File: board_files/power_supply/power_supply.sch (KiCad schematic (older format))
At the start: 4 parts

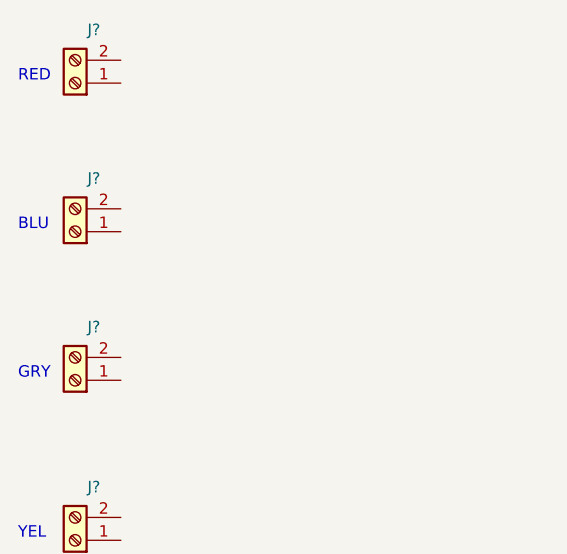
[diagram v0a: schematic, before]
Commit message: Added bridge rectifiers
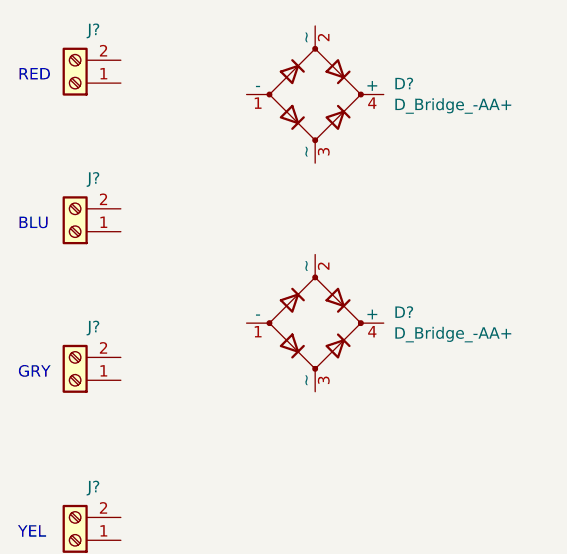
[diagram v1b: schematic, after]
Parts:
- added D? (x2): D_Bridge_-AA+, Diode_THT:Diode_Bridge_32.0x5.6x17.0mm_P10.0mm_P7.5mm, symbol Device:D_Bridge_-AA+
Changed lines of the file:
@@
 EESchema Schematic File Version 4
+LIBS:power_supply-cache
 EELAYER 29 0
 EELAYER END
@@
 Text Notes 3700 4750 0    50   ~ 0
 YEL\n
+$Comp
+L Device:D_Bridge_-AA+ D?
+U 1 1 5EFB3361
+P 5000 2800
+F 0 "D?" H 5344 2846 50  0000 L CNN
+F 1 "D_Bridge_-AA+" H 5344 2755 50  0000 L CNN
+F 2 "Diode_THT:Diode_Bridge_32.0x5.6x17.0mm_P10.0mm_P7.5mm" H 5000 2800 50  0001 C CNN
+F 3 "~" H 5000 2800 50  0001 C CNN
+F 4 "BRIDGE RECT 1PHASE 800V 25A GBJ" H 5000 2800 50  0001 C CNN "Description"
+F 5 "GBJ2508-BP" H 5000 2800 50  0001 C CNN "MPN"
+F 6 "GBJ2508-BPMS-ND" H 5000 2800 50  0001 C CNN "Digikey PN"
+	1    5000 2800
+	1    0    0    -1
+$EndComp
+$Comp
+L Device:D_Bridge_-AA+ D?
+U 1 1 5EFB44A5
+P 5000 3800
+F 0 "D?" H 5344 3846 50  0000 L CNN
+F 1 "D_Bridge_-AA+" H 5344 3755 50  0000 L CNN
+F 2 "Diode_THT:Diode_Bridge_32.0x5.6x17.0mm_P10.0mm_P7.5mm" H 5000 3800 50  0001 C CNN
+F 3 "~" H 5000 3800 50  0001 C CNN
+F 4 "BRIDGE RECT 1PHASE 800V 25A GBJ" H 5000 3800 50  0001 C CNN "Description"
+F 5 "GBJ2508-BP" H 5000 3800 50  0001 C CNN "MPN"
+F 6 "GBJ2508-BPMS-ND" H 5000 3800 50  0001 C CNN "Digikey PN"
+	1    5000 3800
+	1    0    0    -1
+$EndComp
 $EndSCHEMATC

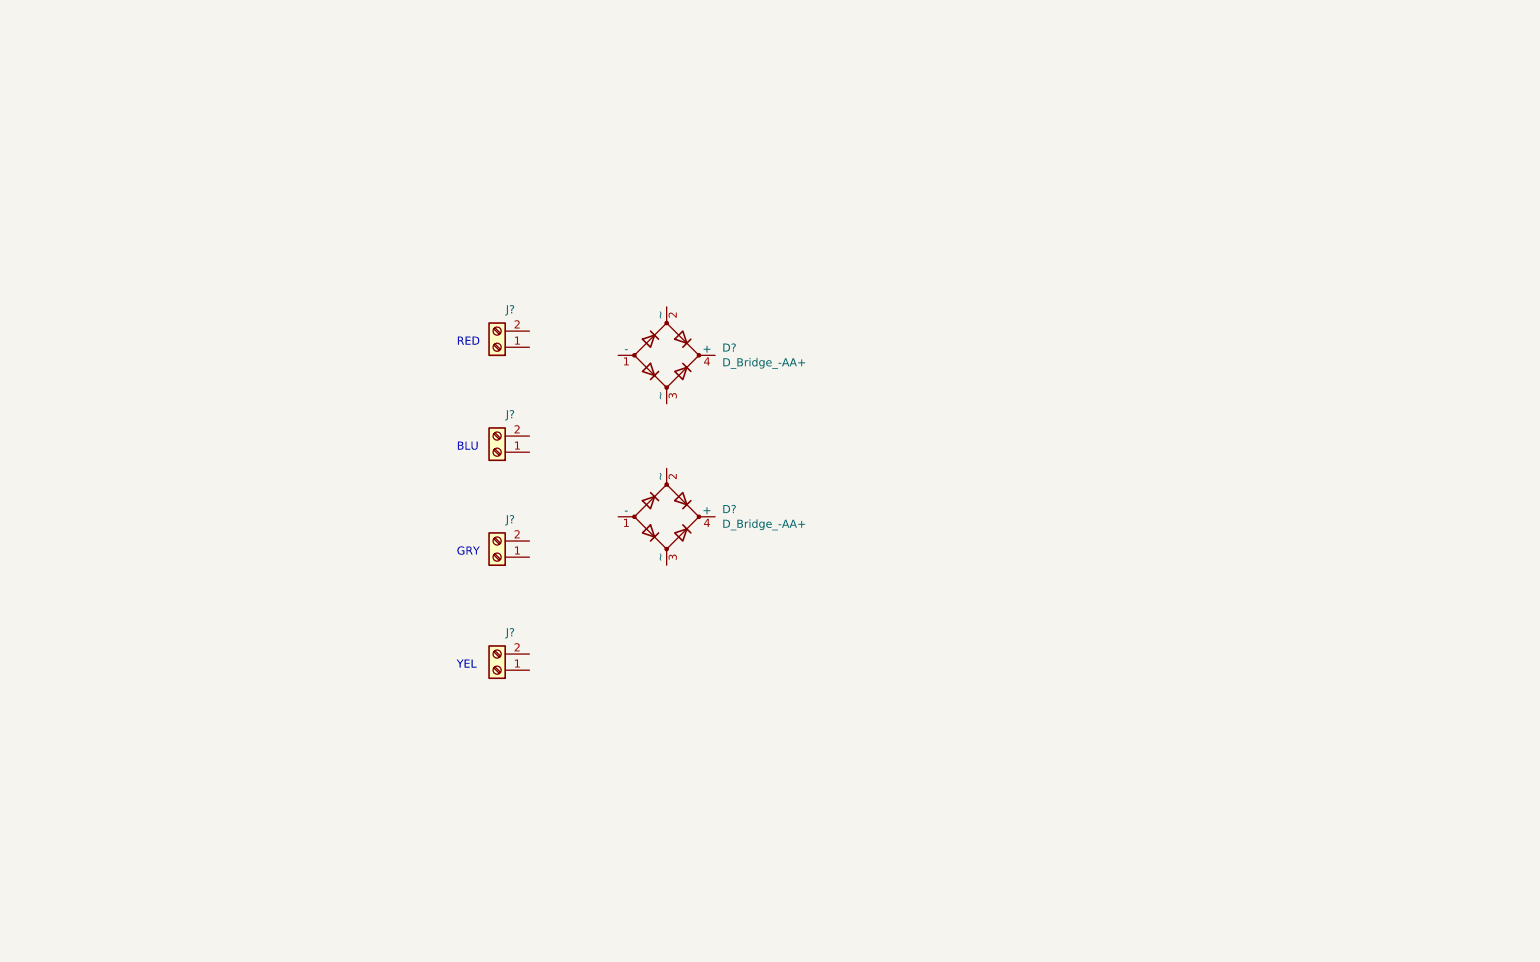
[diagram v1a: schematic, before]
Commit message: Finished adding components to PSU schematic, started wiring
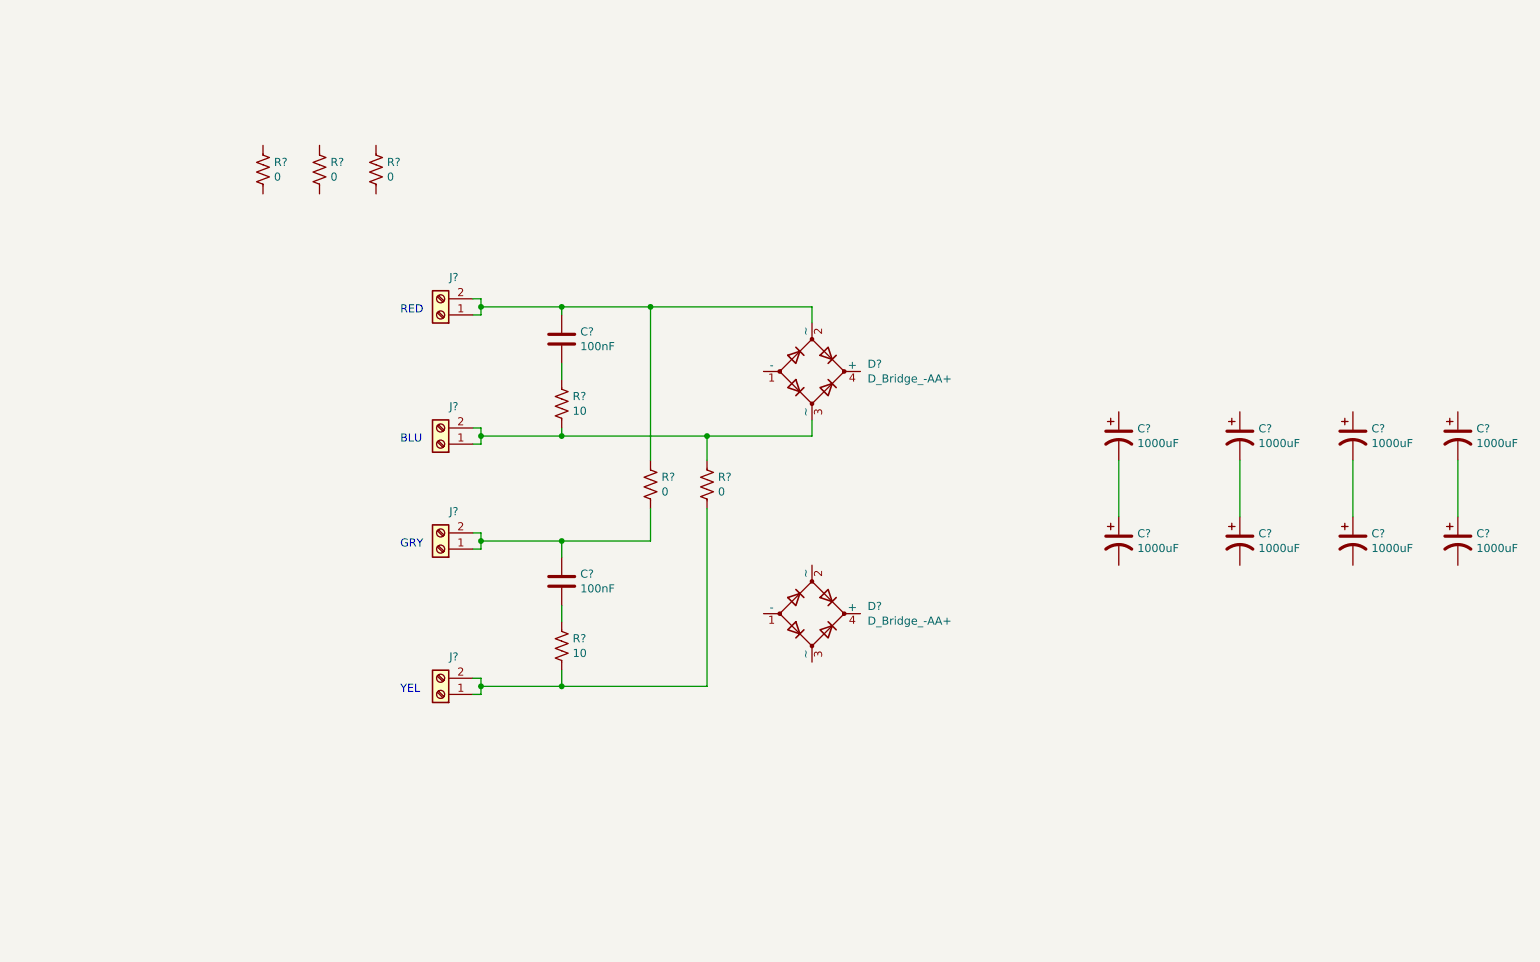
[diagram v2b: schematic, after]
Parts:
- added C? (x8): 1000uF, Capacitor_THT:CP_Radial_D12.5mm_P5.00mm, symbol Device:CP1
- added C? (x2): 100nF, Capacitor_SMD:C_1206_3216Metric, symbol Device:C
- added R? (x2): 10, Resistor_THT:R_Axial_DIN0207_L6.3mm_D2.5mm_P7.62mm_Horizontal, symbol Device:R_US
- added R? (x5): 0, symbol Device:R_US
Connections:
- net at J?.1 (Pin_1): now also D?.2 (~~), J?.2 (Pin_2), C?.1, R?.1
- net at J?.1 (Pin_1): now also D?.3 (~~), J?.2 (Pin_2), R?.1, R?.2
- net at J?.1 (Pin_1): now also J?.2 (Pin_2), C?.1, R?.2
- net at J?.1 (Pin_1): now also J?.2 (Pin_2), R?.2, R?.2
- new net: C?.1, C?.2 (x4)
- new net: C?.2, R?.1 (x2)
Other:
- moved on the sheet: D?, J?

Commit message: finished psu schematic and added front panel
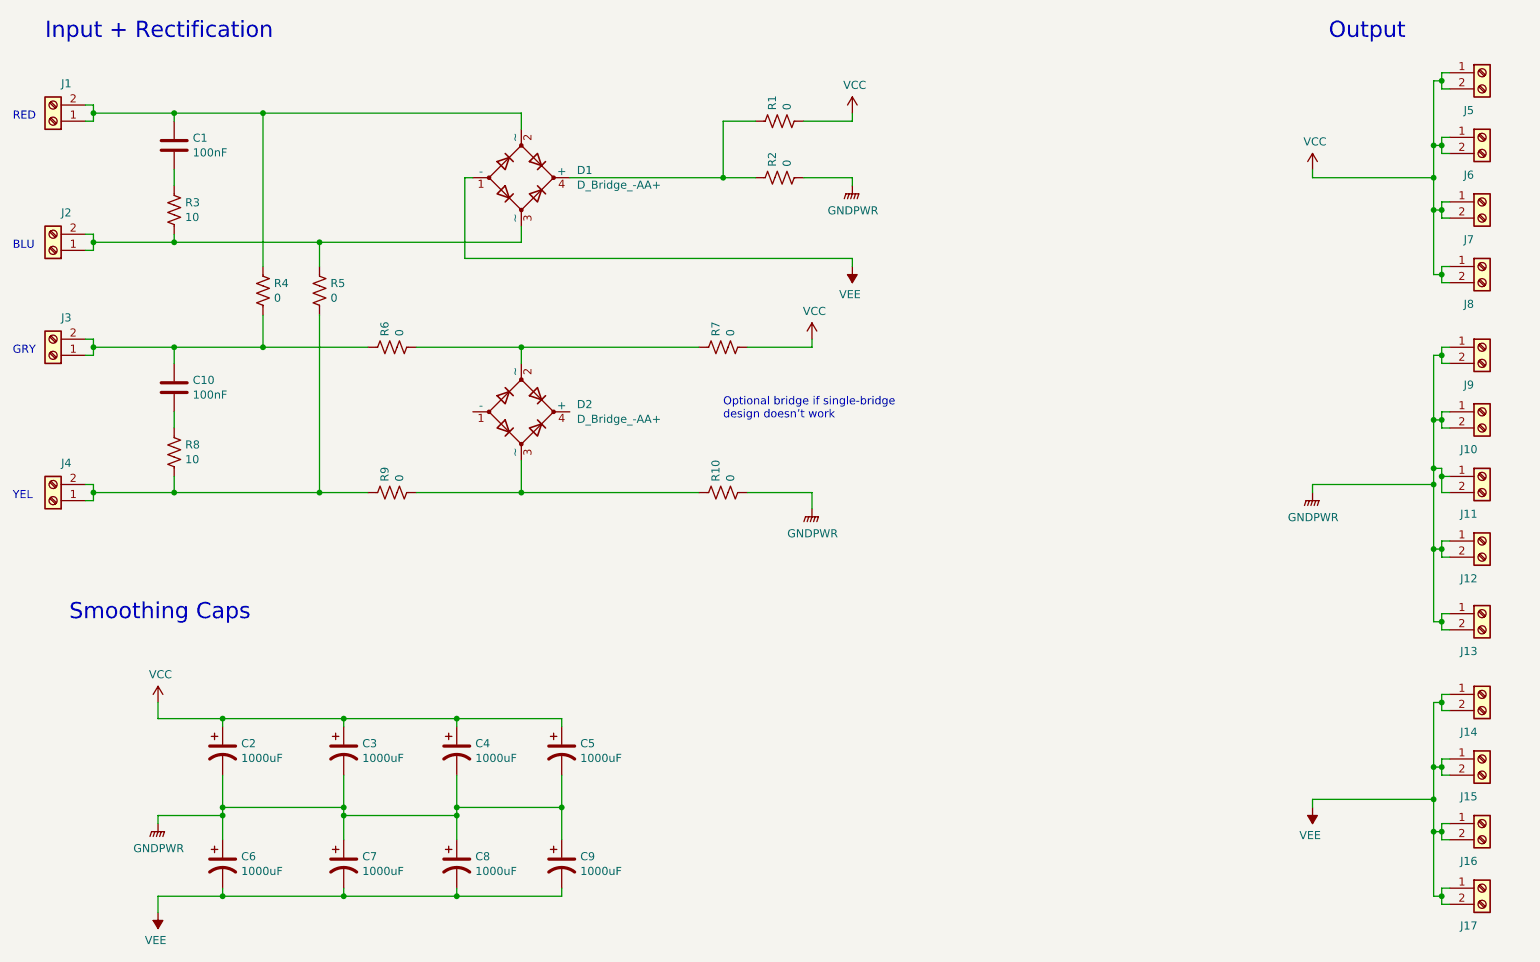
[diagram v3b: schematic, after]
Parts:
- removed R? (x5): 0, symbol Device:R_US
- added J10, J11, J12, J13, J14, J15, J16, J17, J5, J6, J7, J8, J9: Screw_Terminal_01x02, Connector_QC_Blade_User:TE_QC_250_Male_Blade_P5.08, symbol Connector:Screw_Terminal_01x02
- added R1, R10, R2, R4, R5, R6, R7, R9: 0, power_supply:12_Gauge_Jumper, symbol Device:R_US
- gave numbers to parts that had none: 18
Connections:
- net at C1.1, D1.2 (~~), J1.1 (Pin_1)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: now also R4.1
- net at D1.3 (~~), J2.1 (Pin_1), J2.2 (Pin_2)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: now also R5.1
- net at C10.1, J3.1 (Pin_1), J3.2 (Pin_2): now also R4.2, R6.1
- net at J4.1 (Pin_1), J4.2 (Pin_2), R8.2: now also R5.2, R9.1
- net VEE: now reaches D1.1 (-)
- net VEE: now also C6.2, C7.2, C8.2, C9.2, J14.1 (Pin_1), J14.2 (Pin_2), J15.1 (Pin_1), J15.2 (Pin_2), J16.1 (Pin_1), J16.2 (Pin_2), J17.1 (Pin_1), J17.2 (Pin_2)
- net at D1.4 (+): now also R1.1, R2.1
- net at D2.2 (~~): now also R6.2, R7.1
- net at D2.3 (~~): now also R10.1, R9.2
- net VCC: now reaches C2.1
- net VCC: now also C3.1, C4.1, C5.1, J5.1 (Pin_1), J5.2 (Pin_2), J6.1 (Pin_1), J6.2 (Pin_2), J7.1 (Pin_1), J7.2 (Pin_2), J8.1 (Pin_1), J8.2 (Pin_2), R1.2, R7.2
- net GNDPWR: now reaches C2.2, C6.1
- net GNDPWR: now also C3.2, C4.2, C5.2, C7.1, C8.1, C9.1, J10.1 (Pin_1), J10.2 (Pin_2), J11.1 (Pin_1), J11.2 (Pin_2), J12.1 (Pin_1), J12.2 (Pin_2), J13.1 (Pin_1), J13.2 (Pin_2), J9.1 (Pin_1), J9.2 (Pin_2), R10.2, R2.2
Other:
- note added: "Input + Rectification"
- note added: "Optional bridge if single-bridge \ndesign doesn’t work"
- note added: "Output\n"
- note added: "Smoothing Caps\n"
- moved on the sheet: C1, C10, C2, C3, C4, C5, C6, C7, C8, C9, D1, D2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

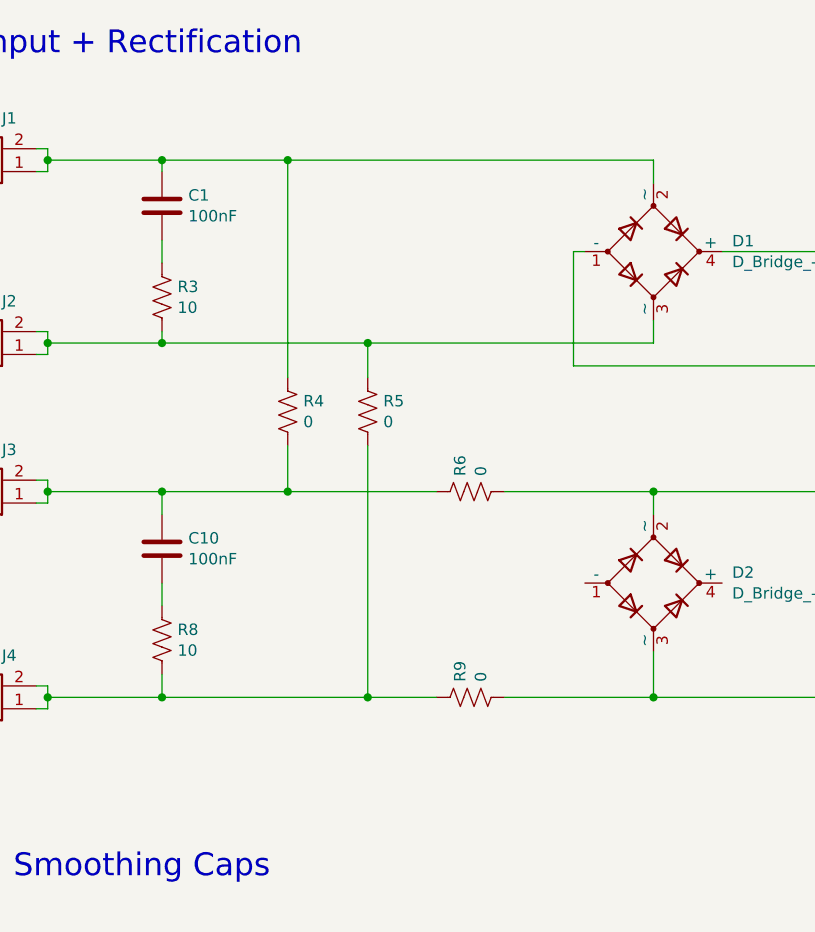
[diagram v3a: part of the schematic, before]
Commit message: rough component placement
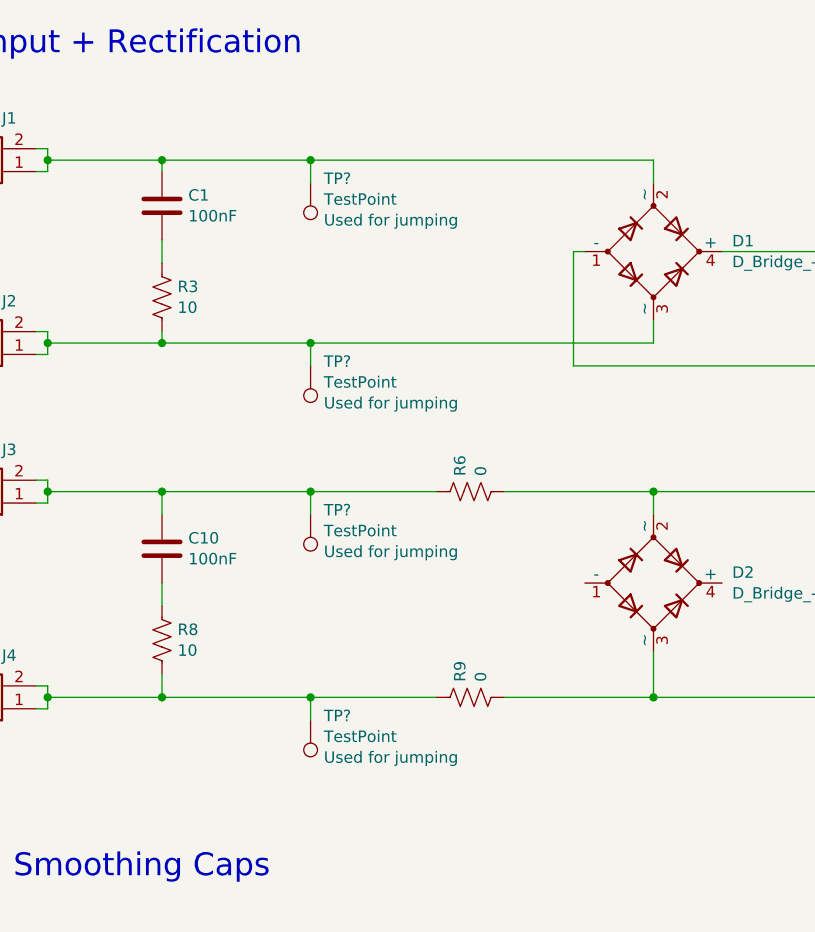
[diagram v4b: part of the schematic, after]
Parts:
- removed R4, R5: 0, power_supply:12_Gauge_Jumper, symbol Device:R_US
- added TP? (x4): TestPoint, power_supply:12_Gauge_Jumper_one_pad, symbol Connector:TestPoint
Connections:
- net at C1.1, D1.2 (~~), J1.1 (Pin_1)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: now also TP?.1
- net at D1.3 (~~), J2.1 (Pin_1), J2.2 (Pin_2)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: now also TP?.1
- net at C10.1, J3.1 (Pin_1), J3.2 (Pin_2)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: now also TP?.1
- net at J4.1 (Pin_1), J4.2 (Pin_2), R8.2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: now also TP?.1
